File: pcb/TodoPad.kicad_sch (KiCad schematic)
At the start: 13 parts, among them SW1 SW_Push, SW10 SW_Push, SW11 SW_Push, SW2 SW_Push, SW3 SW_Push, SW4 SW_Push, SW5 SW_Push, SW6 SW_Push, SW7 SW_Push, SW8 SW_Push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

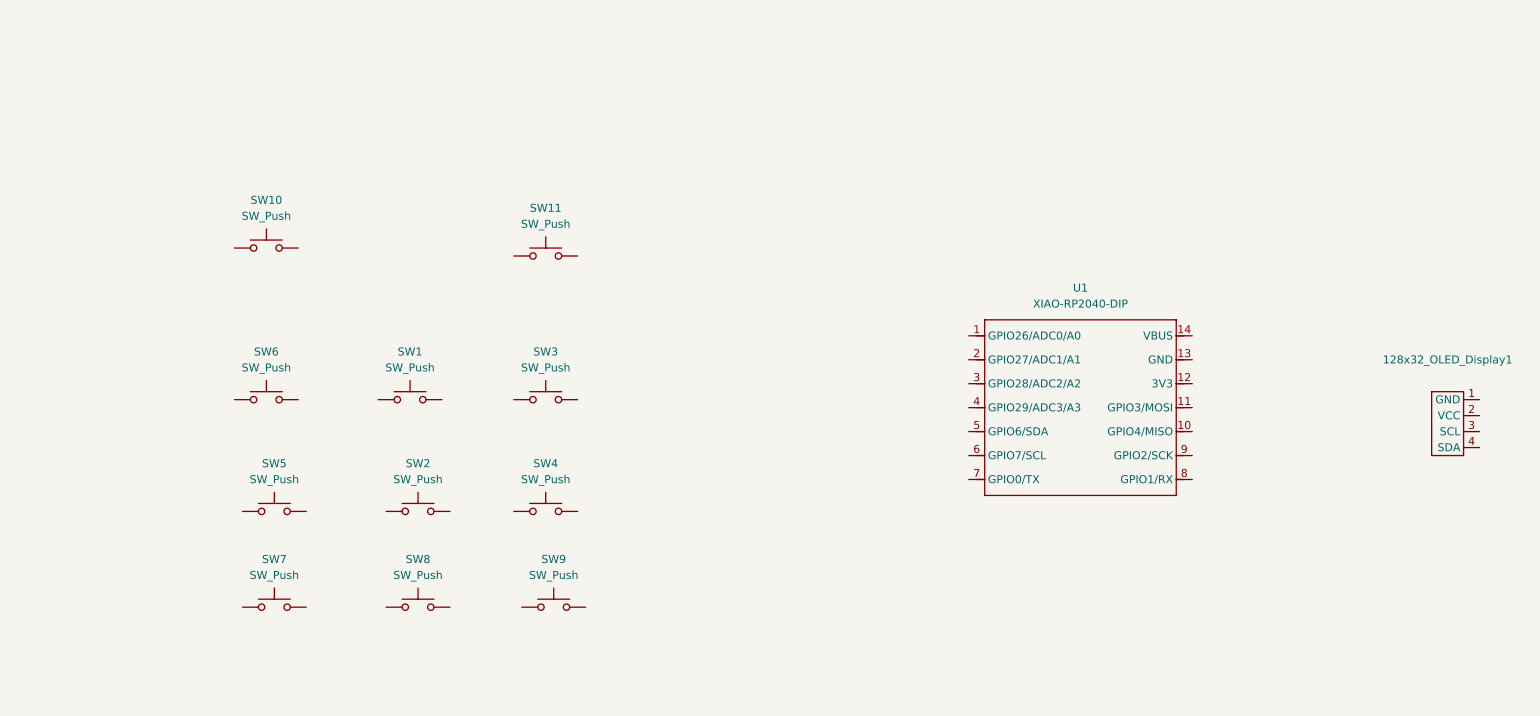
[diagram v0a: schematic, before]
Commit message: Wired up buttons on schematic
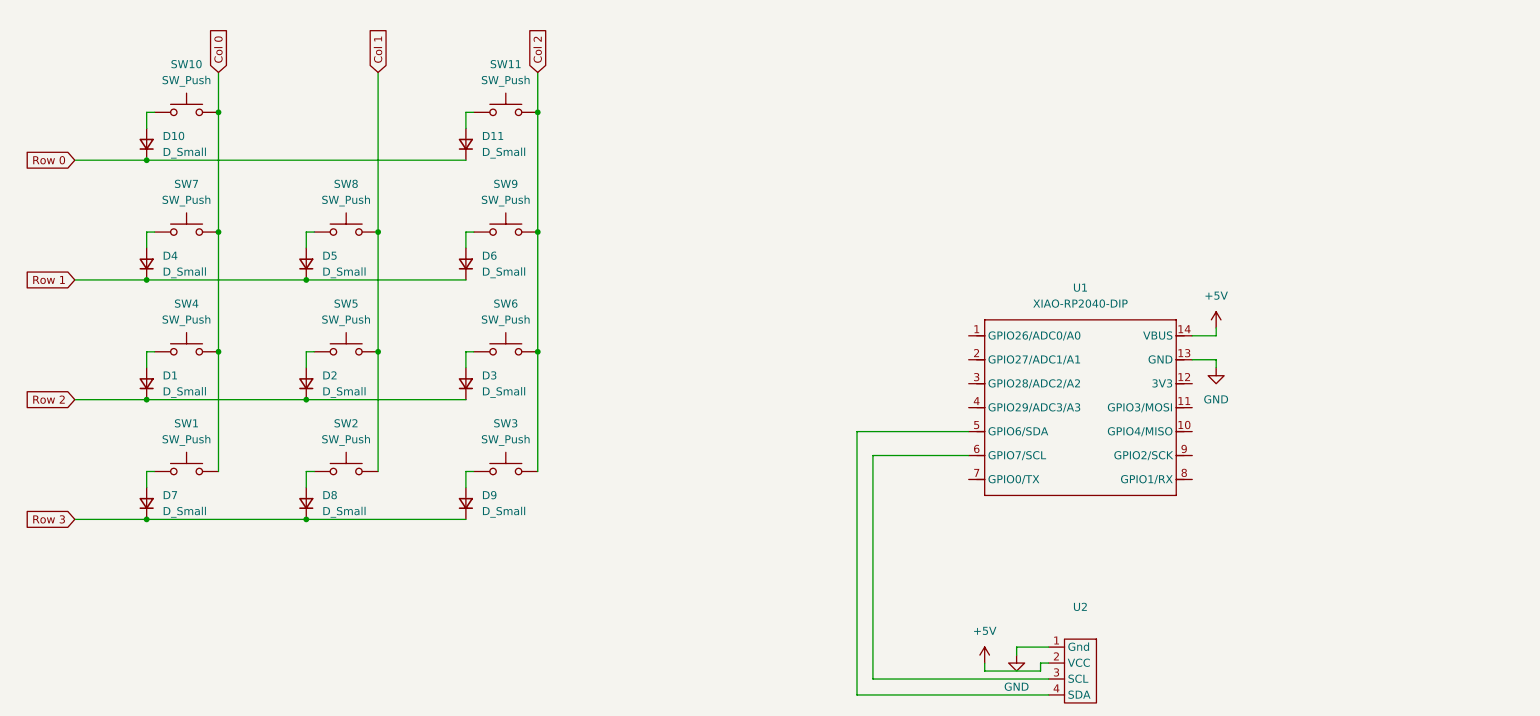
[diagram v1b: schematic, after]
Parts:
- removed 128x32_OLED_Display1: ~, symbol SSD1306_0.91_inch_128x32_OLED_Display:SSD1306_0.91_inch_128x32_OLED_Display
- added D1, D10, D11, D2, D3, D4, D5, D6, D7, D8, D9: D_Small, symbol Device:D_Small
- added U2: ~, 4-pin SSD1306 OLED 128x32:SSD1306-0.91-OLED-4pin-128x32, symbol SSD1306_0.91_inch_128x32_OLED_Display:SSD1306_0.91_inch_128x32_OLED_Display
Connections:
- net at SW4.1: now also D1.2 (A)
- net Col 0: now reaches SW4.2
- net Col 0: now also SW1.2, SW10.2, SW7.2
- net GND: now reaches U1.13 (GND)
- net GND: now also U2.1 (Gnd)
- net +5V: now reaches U1.14 (VBUS)
- net +5V: now also U2.2 (VCC)
- net at U1.5 (GPIO6/SDA): now also U2.4 (SDA)
- net at U1.6 (GPIO7/SCL): now also U2.3 (SCL)
- net at SW1.1: now also D7.2 (A)
- net at SW2.1: now also D8.2 (A)
- net Col 1: now reaches SW2.2
- net Col 1: now also SW5.2, SW8.2
- net at SW10.1: now also D10.2 (A)
- net at SW3.1: now also D9.2 (A)
- net Col 2: now reaches SW3.2
- net Col 2: now also SW11.2, SW6.2, SW9.2
- net at SW7.1: now also D4.2 (A)
- net at SW6.1: now also D3.2 (A)
- net at SW5.1: now also D2.2 (A)
- net at SW8.1: now also D5.2 (A)
- net at SW9.1: now also D6.2 (A)
- net at SW11.1: now also D11.2 (A)
- new net Row 0: D10.1 (K), D11.1 (K)
- new net Row 1: D4.1 (K), D5.1 (K), D6.1 (K)
- new net Row 2: D1.1 (K), D2.1 (K), D3.1 (K)
- new net Row 3: D7.1 (K), D8.1 (K), D9.1 (K)
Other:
- moved on the sheet: SW1, SW10, SW11, SW2, SW3, SW4, SW5, SW6, SW7, SW8, SW9

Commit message: Add the correct number of buttons, updated footprint assignment
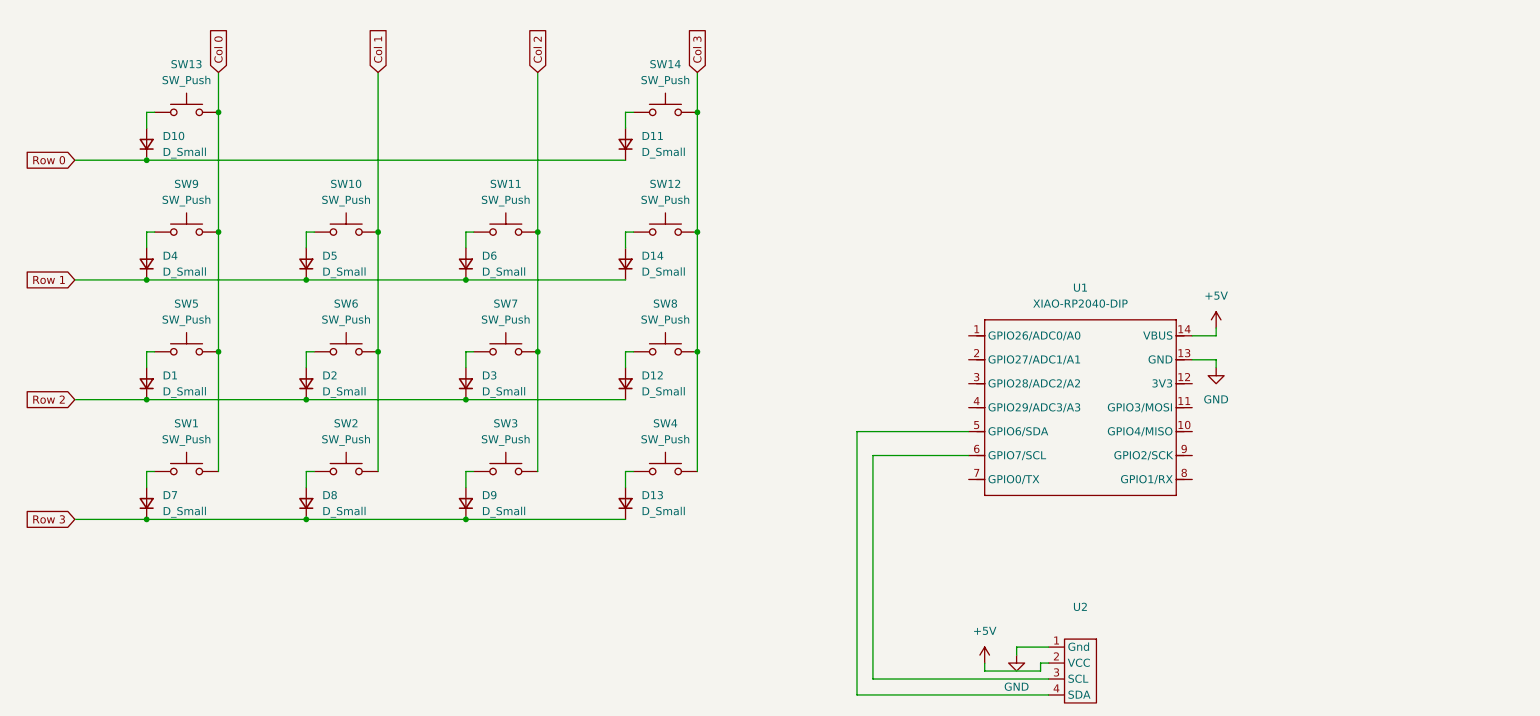
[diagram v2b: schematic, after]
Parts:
- added D12, D13, D14: D_Small, symbol Device:D_Small
- added SW12, SW13, SW14: SW_Push, Button_Switch_Keyboard:SW_Cherry_MX_1.00u_PCB, symbol Switch:SW_Push
- SW1, SW10, SW11, SW2, SW3, SW4, SW5, SW6, SW7, SW8, SW9: footprint (none) -> Button_Switch_Keyboard:SW_Cherry_MX_1.00u_PCB
- U1: footprint Module:MOUDLE14P-XIAO-DIP-SMD -> OPL:XIAO-RP2040-DIP
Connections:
- net Col 0: now also SW5.2, SW9.2, SW13.2; no longer SW10.2, SW4.2, SW7.2
- net Col 1: now also SW10.2, SW6.2; no longer SW5.2, SW8.2
- net Col 2: now also SW7.2; no longer SW6.2, SW9.2
- net Row 1: now also D14.1 (K)
- net Row 2: now also D12.1 (K)
- net Row 3: now also D13.1 (K)
- net at D10.2 (A): now also SW13.1; no longer SW10.1
- net at SW4.1: now also D13.2 (A); no longer D1.2 (A)
- net at D3.2 (A): now also SW7.1; no longer SW6.1
- net at D4.2 (A): now also SW9.1; no longer SW7.1
- net at D6.2 (A): now also SW11.1; no longer SW9.1
- net at D5.2 (A): now also SW10.1; no longer SW8.1
- net at SW5.1: now also D1.2 (A); no longer D2.2 (A)
- net at D11.2 (A): now also SW14.1; no longer SW11.1
- new net: D2.2 (A), SW6.1
- new net: D14.2 (A), SW12.1
- new net: D12.2 (A), SW8.1
- new net Col 3: SW12.2, SW14.2, SW4.2, SW8.2
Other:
- moved on the sheet: D11, SW10, SW11, SW4, SW5, SW6, SW7, SW8, SW9

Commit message: Schematic is done and pcb is organised
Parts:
- D1, D10, D11, D12, D13, D14, D2, D3, D4, D5, D6, D7, D8, D9: footprint (none) -> Diode_THT:D_DO-35_SOD27_P7.62mm_Horizontal
- U2: value ~ -> SSD1306_128x32_OLED_Display
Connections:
- net Col 0: now also U1.11 (GPIO3/MOSI)
- net Col 1: now also U1.10 (GPIO4/MISO)
- net Col 2: now also U1.9 (GPIO2/SCK)
- net Col 3: now also U1.8 (GPIO1/RX)
- net Row 0: now also U1.1 (GPIO26/ADC0/A0)
- net Row 1: now also U1.2 (GPIO27/ADC1/A1)
- net Row 2: now also U1.3 (GPIO28/ADC2/A2)
- net Row 3: now also U1.4 (GPIO29/ADC3/A3)
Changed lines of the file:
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@@
+		)
+	)
+	(global_label "Col 3"
+		(shape input)
+		(at 203.2 115.57 0)
+		(fields_autoplaced yes)
+		(effects
+			(font
+				(size 1.27 1.27)
+			)
+			(justify left)
+		)
+		(property "Intersheetrefs" "${INTERSHEET_REFS}"
+			(at 211.4465 115.57 0)
+			(effects
+				(font
+					(size 1.27 1.27)
+				)
+				(justify left)
+				(hide yes)
+			)
 		)
 	)
@@
 		)
 	)
+	(global_label "Row 2"
+		(shape input)
+		(at 167.64 100.33 180)
+		(fields_autoplaced yes)
+		(effects
+			(font
+				(size 1.27 1.27)
+			)
+			(justify right)
+		)
+		(property "Intersheetrefs" "${INTERSHEET_REFS}"
+			(at 158.7282 100.33 0)
+			(effects
+				(font
+					(size 1.27 1.27)
+				)
+				(justify right)
+				(hide yes)
+			)
+		)
+	)
 	(global_label "Col 2"
 		(shape input)
@@
 		)
 	)
+	(global_label "Row 1"
+		(shape input)
+		(at 167.64 96.52 180)
+		(fields_autoplaced yes)
+		(effects
+			(font
+				(size 1.27 1.27)
+			)
+			(justify right)
+		)
+		(property "Intersheetrefs" "${INTERSHEET_REFS}"
+			(at 158.7282 96.52 0)
+			(effects
+				(font
+					(size 1.27 1.27)
+				)
+				(justify right)
+				(hide yes)
+			)
+		)
+	)
+	(global_label "Col 2"
+		(shape input)
+		(at 203.2 111.76 0)
+		(fields_autoplaced yes)
+		(effects
+			(font
+				(size 1.27 1.27)
+			)
+			(justify left)
+		)
+		(property "Intersheetrefs" "${INTERSHEET_REFS}"
+			(at 211.4465 111.76 0)
+			(effects
+				(font
+					(size 1.27 1.27)
+				)
+				(justify left)
+				(hide yes)
+			)
+		)
+	)
 	(global_label "Row 0"
 		(shape input)
@@
 		)
 	)
+	(global_label "Row 0"
+		(shape input)
+		(at 167.64 92.71 180)
+		(fields_autoplaced yes)
+		(effects
+			(font
+				(size 1.27 1.27)
+			)
+			(justify right)
+		)
+		(property "Intersheetrefs" "${INTERSHEET_REFS}"
+			(at 158.7282 92.71 0)
+			(effects
+				(font
+					(size 1.27 1.27)
+				)
+				(justify right)
+				(hide yes)
+			)
+		)
+	)
 	(global_label "Row 1"
 		(shape input)
@@
 	(global_label "Row 3"
 		(shape input)
-		(at 25.4 121.92 180)
+		(at 167.64 104.14 180)
 		(fields_autoplaced yes)
 		(effects
@@
 		)
 		(property "Intersheetrefs" "${INTERSHEET_REFS}"
+			(at 158.7282 104.14 0)
+			(effects
+				(font
+					(size 1.27 1.27)
+				)
+				(justify right)
+				(hide yes)
+			)
+		)
+	)
+	(global_label "Col 0"
+		(shape input)
+		(at 203.2 104.14 0)
+		(fields_autoplaced yes)
+		(effects
+			(font
+				(size 1.27 1.27)
+			)
+			(justify left)
+		)
+		(property "Intersheetrefs" "${INTERSHEET_REFS}"
+			(at 211.4465 104.14 0)
+			(effects
+				(font
+					(size 1.27 1.27)
+				)
+				(justify left)
+				(hide yes)
+			)
+		)
+	)
+	(global_label "Col 1"
+		(shape input)
+		(at 203.2 107.95 0)
+		(fields_autoplaced yes)
+		(effects
+			(font
+				(size 1.27 1.27)
+			)
+			(justify left)
+		)
+		(property "Intersheetrefs" "${INTERSHEET_REFS}"
+			(at 211.4465 107.95 0)
+			(effects
+				(font
+					(size 1.27 1.27)
+				)
+				(justify left)
+				(hide yes)
+			)
+		)
+	)
+	(global_label "Row 3"
+		(shape input)
+		(at 25.4 121.92 180)
+		(fields_autoplaced yes)
+		(effects
+			(font
+				(size 1.27 1.27)
+			)
+			(justify right)
+		)
+		(property "Intersheetrefs" "${INTERSHEET_REFS}"
 			(at 16.4882 121.92 0)
 			(effects
@@
 			)
 		)
-		(property "Footprint" ""
+		(property "Footprint" "Diode_THT:D_DO-35_SOD27_P7.62mm_Horizontal"
 			(at 62.23 119.38 90)
 			(effects
@@
 			)
 		)
-		(property "Footprint" ""
+		(property "Footprint" "Diode_THT:D_DO-35_SOD27_P7.62mm_Horizontal"
 			(at 36.83 62.23 90)
 			(effects
@@
 			)
 		)
-		(property "Footprint" ""
+		(property "Footprint" "Diode_THT:D_DO-35_SOD27_P7.62mm_Horizontal"
 			(at 87.63 100.33 90)
 			(effects
@@
 	)
 	(symbol
+		(lib_name "SSD1306_0.91_inch_128x32_OLED_Display_1")
 		(lib_id "SSD1306_0.91_inch_128x32_OLED_Display:SSD1306_0.91_inch_128x32_OLED_Display")
 		(at 185.42 139.7 0)
@@
 			)
 		)
-		(property "Value" "~"
+		(property "Value" "SSD1306_128x32_OLED_Display"
 			(at 185.42 138.43 0)
 			(effects
@@
 		(pin "4"
 		)
-		(pin "1"
-		)
 		(pin "3"
+		)
+		(pin "1"
 		)
 		(instances
@@
 			)
 		)
-		(property "Footprint" ""
+		(property "Footprint" "Diode_THT:D_DO-35_SOD27_P7.62mm_Horizontal"
 			(at 36.83 119.38 90)
 			(effects
@@
 			)
 		)
-		(property "Footprint" ""
+		(property "Footprint" "Diode_THT:D_DO-35_SOD27_P7.62mm_Horizontal"
 			(at 36.83 100.33 90)
 			(effects
@@
 			)
 		)
-		(property "Footprint" ""
+		(property "Footprint" "Diode_THT:D_DO-35_SOD27_P7.62mm_Horizontal"
 			(at 87.63 81.28 90)
 			(effects
@@
 			)
 		)
-		(property "Footprint" ""
+		(property "Footprint" "Diode_THT:D_DO-35_SOD27_P7.62mm_Horizontal"
 			(at 113.03 81.28 90)
 			(effects
@@
 			)
 		)
-		(property "Footprint" ""
+		(property "Footprint" "Diode_THT:D_DO-35_SOD27_P7.62mm_Horizontal"
 			(at 62.23 81.28 90)
 			(effects
@@
 			)
 		)
-		(property "Footprint" ""
+		(property "Footprint" "Diode_THT:D_DO-35_SOD27_P7.62mm_Horizontal"
 			(at 87.63 119.38 90)
 			(effects
@@
 			)
 		)
-		(property "Footprint" ""
+		(property "Footprint" "Diode_THT:D_DO-35_SOD27_P7.62mm_Horizontal"
 			(at 36.83 81.28 90)
 			(effects
@@
 			)
 		)
-		(property "Footprint" ""
+		(property "Footprint" "Diode_THT:D_DO-35_SOD27_P7.62mm_Horizontal"
 			(at 113.03 62.23 90)
 			(effects
@@
 			)
 		)
-		(property "Footprint" ""
+		(property "Footprint" "Diode_THT:D_DO-35_SOD27_P7.62mm_Horizontal"
 			(at 113.03 100.33 90)
 			(effects
@@
 			)
 		)
-		(property "Footprint" ""
+		(property "Footprint" "Diode_THT:D_DO-35_SOD27_P7.62mm_Horizontal"
 			(at 62.23 100.33 90)
 			(effects
@@
 			)
 		)
-		(property "Footprint" ""
+		(property "Footprint" "Diode_THT:D_DO-35_SOD27_P7.62mm_Horizontal"
 			(at 113.03 119.38 90)
 			(effects
